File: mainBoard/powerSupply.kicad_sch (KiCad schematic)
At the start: 64 parts, among them J1 1366005, SW1 SW_SPST, U1 RT6255BHGJ8F, U2 RT9059GSP, U3 RT9059GSP, U4 TPS2041B

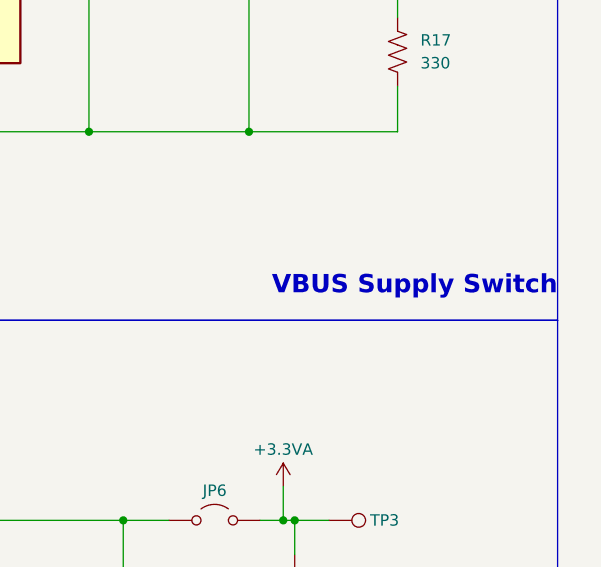
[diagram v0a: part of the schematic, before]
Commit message: replace piezo with actual speaker
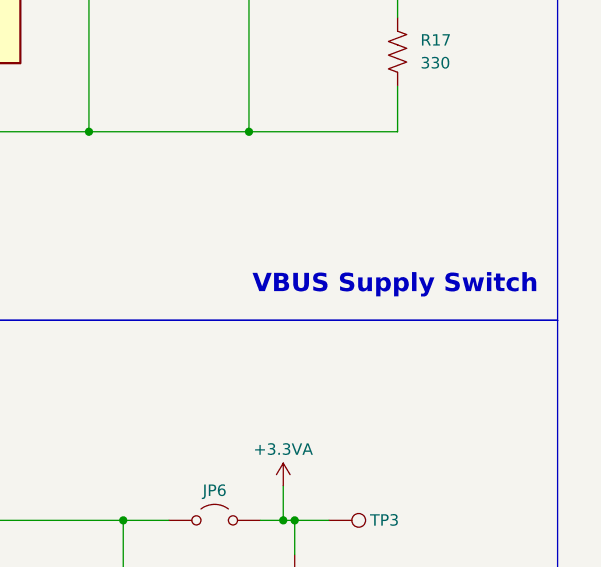
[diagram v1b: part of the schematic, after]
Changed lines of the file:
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@@
 	(text "VBUS Supply Switch"
 		(exclude_from_sim no)
-		(at 375.285 156.845 0)
+		(at 373.126 156.718 0)
 		(effects
 			(font

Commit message: working on layout
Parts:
- removed TP1, TP2: TestPoint, TestPoint:TestPoint_Pad_4.0x4.0mm, symbol Connector:TestPoint
- added C54: 22uF, Capacitor_SMD:C_1206_3216Metric_Pad1.33x1.80mm_HandSolder, symbol Device:C
- C4: footprint Capacitor_SMD:C_0603_1608Metric_Pad1.08x0.95mm_HandSolder -> Capacitor_SMD:C_0402_1005Metric_Pad0.74x0.62mm_HandSolder
- TP22: footprint TestPoint:TestPoint_Pad_4.0x4.0mm -> TestPoint:TestPoint_Pad_D2.0mm
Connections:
- net +12V: now also C54.1
- net GND: now also C54.2
- net L1-120VAC: now also J1.3 (Pin_3); no longer J1.1 (Pin_1)
- net LN: now also J1.1 (Pin_1); no longer J1.3 (Pin_3)
- net +3v3_Vout: now reaches C5.1, C7.1, JP1.1 (A), R1.2, R3.1, U2.6 (VOUT)
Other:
- moved on the sheet: J1

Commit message: work on layout, change to larger inductor
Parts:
- L1: footprint Inductor_SMD:L_1008_2520Metric_Pad1.43x2.20mm_HandSolder -> Inductor_SMD:L_Coilcraft_XAL7030-472; part number MAMK2520T2R2M -> 7440700047
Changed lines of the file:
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@@
 			)
 		)
-		(property "Footprint" "Inductor_SMD:L_1008_2520Metric_Pad1.43x2.20mm_HandSolder"
+		(property "Footprint" "Inductor_SMD:L_Coilcraft_XAL7030-472"
 			(at 123.19 109.22 0)
 			(hide yes)
@@
 			)
 		)
-		(property "part number" "MAMK2520T2R2M"
+		(property "part number" "7440700047"
 			(at 123.19 109.22 90)
 			(hide yes)

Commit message: add guard ring for analog and also move stuff around
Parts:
- removed TP4: TestPoint, TestPoint:TestPoint_Pad_4.0x4.0mm, symbol Connector:TestPoint
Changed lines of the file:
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@@
 	)
 	(junction
-		(at 361.95 212.09)
-		(diameter 0)
-		(color 0 0 0 0)
-	)
-	(junction
 		(at 186.69 109.22)
 		(diameter 0)
@@
 	(wire
 		(pts
-			(xy 361.95 212.09) (xy 365.76 212.09)
-		)
-		(stroke
-			(width 0)
-			(type default)
-		)
-	)
-	(wire
-		(pts
 			(xy 250.19 212.09) (xy 234.95 212.09)
 		)
@@
 					(unit 1)
 				)
-			)
-		)
-	)
-	(symbol
-		(lib_id "Connector:TestPoint")
-		(at 365.76 212.09 270)
-		(unit 1)
-		(body_style 1)
-		(exclude_from_sim no)
-		(in_bom yes)
-		(on_board yes)
-		(in_pos_files yes)
-		(dnp no)
-		(property "Reference" "TP4"
-			(at 370.332 212.09 90)
-			(show_name no)
-			(do_not_autoplace no)
-			(effects
-				(font
-					(size 1.27 1.27)
-				)
-				(justify left)
-			)
-		)
-		(property "Value" "TestPoint"
-			(at 370.84 213.3599 90)
-			(hide yes)
-			(show_name no)
-			(do_not_autoplace no)
-			(effects
-				(font
-					(size 1.27 1.27)
-				)
-				(justify left)
-			)
-		)
-		(property "Footprint" "TestPoint:TestPoint_Pad_4.0x4.0mm"
-			(at 365.76 217.17 0)
-			(hide yes)
-			(show_name no)
-			(do_not_autoplace no)
-			(effects
-				(font
-					(size 1.27 1.27)
-				)
-			)
-		)
-		(property "Datasheet" ""
-			(at 365.76 217.17 0)
-			(hide yes)
-			(show_name no)
-			(do_not_autoplace no)
-			(effects
-				(font
-					(size 1.27 1.27)
-				)
-			)
-		)
-		(property "Description" "test point"
-			(at 365.76 212.09 0)
-			(hide yes)
-			(show_name no)
-			(do_not_autoplace no)
-			(effects
-				(font
-					(size 1.27 1.27)
-				)
-			)
-		)
-		(pin "1"
-		)
-		(instances
-			(project "mainBoard"
-				(path "/0650c7a8-acba-429c-9f8e-eec0baf0bc1c/fede4c36-00cc-4d3d-b71c-5243ba232202/f08096be-4241-44f0-80c6-822a4bb8e386"
-					(reference "TP4")
-					(unit 1)
-				)

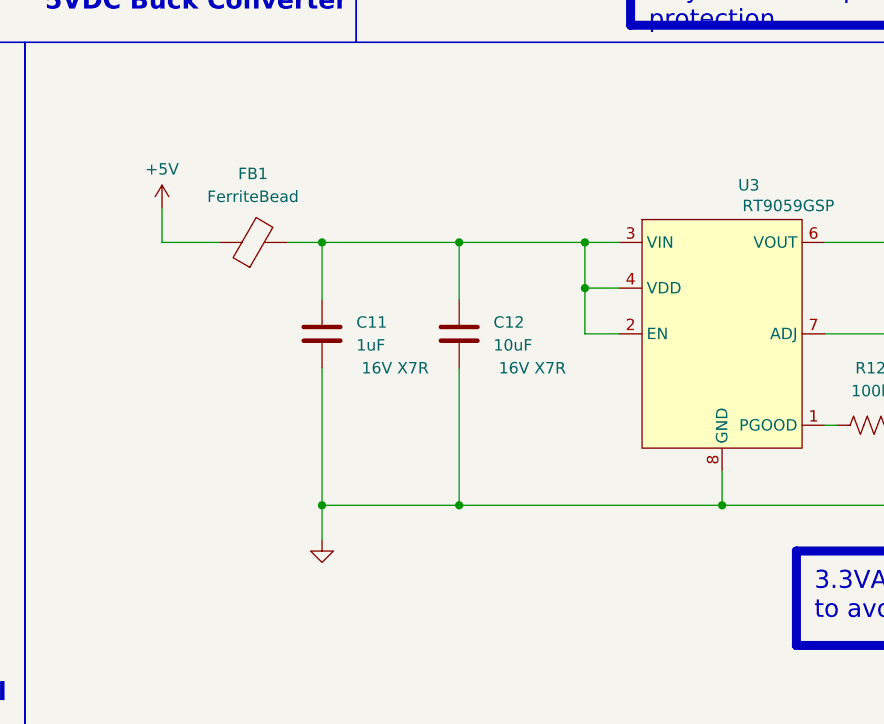
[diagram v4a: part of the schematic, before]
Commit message: layout 3v3a ldo
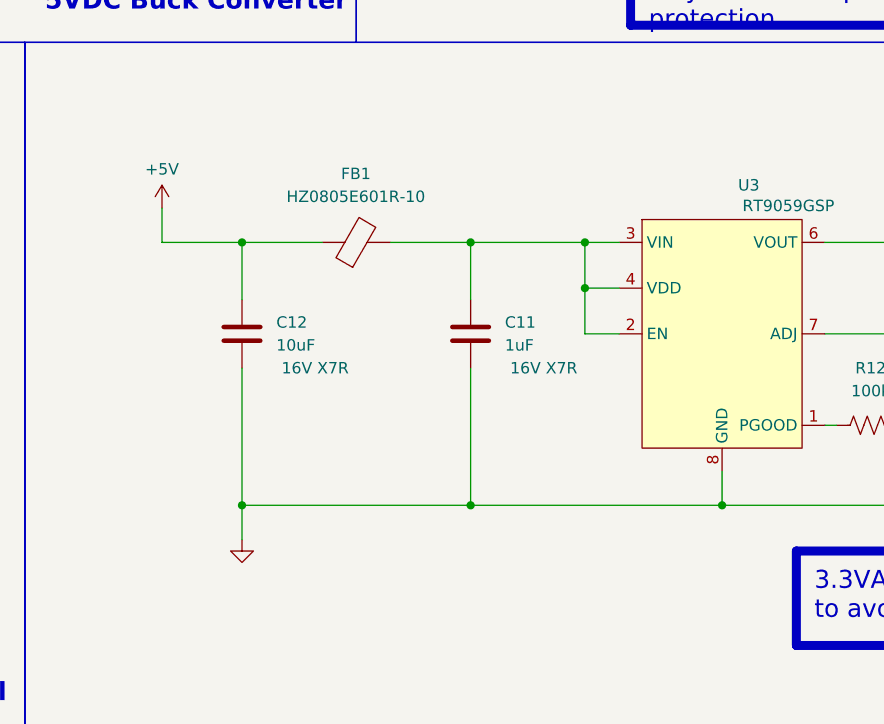
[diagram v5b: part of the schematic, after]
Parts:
- FB1: value FerriteBead -> HZ0805E601R-10; footprint (none) -> Inductor_SMD:L_0805_2012Metric_Pad1.05x1.20mm_HandSolder
- TP3: footprint TestPoint:TestPoint_Pad_4.0x4.0mm -> TestPoint:TestPoint_Pad_2.0x2.0mm
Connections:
- net +5V: now also C12.1
- net at C11.1, FB1.2, U3.2 (EN)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: no longer C12.1
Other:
- moved on the sheet: C11, C12, FB1
